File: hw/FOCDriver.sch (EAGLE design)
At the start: 113 parts, among them IC1 LM258DR2G, IC2 LM258DR2G, Q1 BC817, Q2 BC817, Q3 BC817, Q4 BC817, Q5 BC817, Q6 BC817, U1 SN74LVC2G17, U2 AO4606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

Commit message: LMV321
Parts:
- removed IC1, IC2: LM258DR2G, SparkFun-IC-Amplifiers:OPAMP-DUALU
- added C27, C28: 0.1uF, SparkFun-Capacitors:1.0UF-0805-25V-10%
- added U10, U11, U8, U9: LMV321SQ3T2G, LMV321SQ3T2G:LMV321SQ3T2G
- R23: value 1K 1% -> 5.6K
- R24: value 1K 1% -> 10K; device SparkFun-Resistors:RESISTOR0805 -> pot:TRIM_US-CT6
- R35, R36: value 10K 1% -> 1K 1%
- R46: value 5.6K -> 220
- R47: value 10K -> 10K 1%; device pot:TRIM_US-CT6 -> SparkFun-Resistors:RESISTOR0805
- R48: value 220 -> 10K 1%
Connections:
- net 5V: now also R23.2; no longer R46.2
- net AGND: now also C27.2, C28.2, R48.1, U10.GND, U11.GND, U8.GND, U9.GND; no longer IC1G3.P$V-, IC2G3.P$V-, R36.1
- net DGND: now also R24.A; no longer R47.A
- net GND: now also R29.1; no longer R27.1
- net H1O: now also R46.2; no longer R48.2
- net ICOM: now also R27.1, R30.1; no longer R23.1, R28.1
- net IU: now also R26.1; no longer R24.1
- net IV: now also R28.1; no longer R26.1
- net N$11: now also R25.2, R31.1; no longer R23.2, R29.1
- net N$12: now also R26.2, R32.1; no longer R24.2, R30.1
- net N$13: now also R31.2, U8.-IN; no longer IC2G2.-IN, R29.2
- net N$14: now also R27.2, R33.1; no longer R25.2, R31.1
- net N$15: now also R32.2, R40.1, U8.+IN; no longer IC2G2.+IN, R30.2, R41.1
- net N$16: now also U8.OUT; no longer IC2G2.OUT
- net N$17: now also R28.2, R34.1; no longer R26.2, R32.1
- net N$18: now also C27.1, R47.1, R48.2, U11.+IN; no longer C18.1, IC1G2.+IN, R35.1, R36.2
- net N$19: now also R33.2, U9.-IN; no longer IC1G1.-IN, R31.2
- net N$20: now also R34.2, R41.1, U9.+IN; no longer IC1G1.+IN, R32.2, R42.1
- net N$21: now also U9.OUT; no longer IC1G1.OUT
- net N$22: now also R29.2, R35.1; no longer R27.2, R33.1
- net N$23: now also R30.2, R36.1; no longer R28.2, R34.1
- net N$24: now also R35.2, U10.-IN; no longer IC2G1.-IN, R33.2
- net N$25: now also R36.2, R42.1, U10.+IN; no longer IC2G1.+IN, R34.2, R40.1
- net N$26: now also U10.OUT; no longer IC2G1.OUT
- net N$33: now also R46.1; no longer R48.1
- net N$4: now also R23.1, R24.E; no longer R46.1, R47.E
- net POT: now also R24.S; no longer R47.S
- net PWRDIV: now also R47.2; no longer R35.2
- net VDDA: now also C18.1, C28.1, U10.VCC, U11.VCC, U8.VCC, U9.VCC; no longer IC1G3.P$V+, IC2G3.P$V+
- net VREF: now also U11.-IN, U11.OUT; no longer IC1G2.-IN, IC1G2.OUT
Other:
- moved on the sheet: C17, C18, C19, C20, C23, C24, C26, R23, R25, R26, R27, R28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

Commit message: layout
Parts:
- removed J7: (no value), SparkFun-Connectors:CONN_06SILK_FEMALE_PTH
- added J10: (no value), SparkFun-Connectors:CONN_02
- added J11: (no value), SparkFun-Connectors:CONN_05
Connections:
- net DGND: now also J10.2, J11.5; no longer J7.6
- net IMOTORA: now also J11.3; no longer J7.3
- net IMOTORB: now also J11.1; no longer J7.1
- net IMOTORBUS: now also J11.2; no longer J7.2
- net LEDJP1: now also J10.1; no longer J7.5
- net POT: now also J11.4; no longer J7.4
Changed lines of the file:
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@@
 <clearance class="4" value="0.3048"/>
+</class>
+<class number="5" name="5V" width="0.508" drill="0.4064">
+<clearance class="5" value="0.3048"/>
 </class>
 </classes>
@@
 <part name="C7" library="SparkFun-Capacitors" deviceset="1.0UF" device="-0805-25V-10%" value="0.1uF"/>
 <part name="C4" library="SparkFun-Capacitors" deviceset="1.0UF" device="-0805-25V-10%" value="0.1uF"/>
-<part name="J7" library="SparkFun-Connectors" deviceset="CONN_06" device="SILK_FEMALE_PTH"/>
 <part name="C5" library="rcl" deviceset="CPOL-US" device="E5-10.5" value="220uF/63V"/>
 <part name="C11" library="rcl" deviceset="CPOL-US" device="E5-10.5" value="220uF/63V"/>
@@
 <part name="G10" library="SparkFun-PowerSymbols" deviceset="AGND" device=""/>
 <part name="C28" library="SparkFun-Capacitors" deviceset="1.0UF" device="-0805-25V-10%" value="0.1uF"/>
+<part name="J10" library="SparkFun-Connectors" deviceset="CONN_02" device=""/>
+<part name="GND23" library="SparkFun-PowerSymbols" deviceset="DGND" device=""/>
+<part name="J11" library="SparkFun-Connectors" deviceset="CONN_05" device=""/>
 </parts>
 <sheets>
@@
 <instance part="C7" gate="G$1" x="99.06" y="53.34"/>
 <instance part="C4" gate="G$1" x="60.96" y="53.34"/>
-<instance part="J7" gate="G$1" x="226.06" y="68.58" rot="R180"/>
 <instance part="C5" gate="G$1" x="76.2" y="157.48"/>
 <instance part="C11" gate="G$1" x="152.4" y="157.48"/>
@@
 <instance part="X2" gate="-2" x="193.04" y="48.26" rot="R180"/>
 <instance part="X2" gate="-3" x="193.04" y="53.34" rot="R180"/>
+<instance part="J10" gate="G$1" x="195.58" y="68.58" rot="R180"/>
+<instance part="GND23" gate="G$1" x="182.88" y="60.96"/>
+<instance part="J11" gate="G$1" x="228.6" y="68.58" rot="R180"/>
 </instances>
 <busses>
@@
 <segment>
 <pinref part="GND18" gate="G$1" pin="GND"/>
-<wire x1="213.36" y1="58.42" x2="213.36" y2="60.96" width="0.1524" layer="91"/>
-<pinref part="J7" gate="G$1" pin="6"/>
-<wire x1="213.36" y1="60.96" x2="220.98" y2="60.96" width="0.1524" layer="91"/>
+<wire x1="213.36" y1="58.42" x2="213.36" y2="63.5" width="0.1524" layer="91"/>
+<wire x1="213.36" y1="63.5" x2="220.98" y2="63.5" width="0.1524" layer="91"/>
+<pinref part="J11" gate="G$1" pin="5"/>
 </segment>
 <segment>
@@
 <wire x1="205.74" y1="96.52" x2="205.74" y2="99.06" width="0.1524" layer="91"/>
 <pinref part="GND17" gate="G$1" pin="GND"/>
+</segment>
+<segment>
+<pinref part="J10" gate="G$1" pin="2"/>
+<pinref part="GND23" gate="G$1" pin="GND"/>
+<wire x1="187.96" y1="66.04" x2="182.88" y2="66.04" width="0.1524" layer="91"/>
+<wire x1="182.88" y1="66.04" x2="182.88" y2="63.5" width="0.1524" layer="91"/>
 </segment>
 </net>
@@
 <label x="215.9" y="73.66" size="1.27" layer="95" rot="R180" xref="yes"/>
 <wire x1="215.9" y1="73.66" x2="220.98" y2="73.66" width="0.1524" layer="91"/>
-<pinref part="J7" gate="G$1" pin="1"/>
+<pinref part="J11" gate="G$1" pin="1"/>
 </segment>
 </net>
@@
 <label x="215.9" y="68.58" size="1.27" layer="95" rot="R180" xref="yes"/>
 <wire x1="215.9" y1="68.58" x2="220.98" y2="68.58" width="0.1524" layer="91"/>
-<pinref part="J7" gate="G$1" pin="3"/>
+<pinref part="J11" gate="G$1" pin="3"/>
 </segment>
 </net>
@@
 <label x="215.9" y="66.04" size="1.27" layer="95" rot="R180" xref="yes"/>
 <wire x1="215.9" y1="66.04" x2="220.98" y2="66.04" width="0.1524" layer="91"/>
-<pinref part="J7" gate="G$1" pin="4"/>
+<pinref part="J11" gate="G$1" pin="4"/>
 </segment>
 </net>
@@
 <wire x1="220.98" y1="71.12" x2="215.9" y2="71.12" width="0.1524" layer="91"/>
 <label x="215.9" y="71.12" size="1.27" layer="95" rot="R180" xref="yes"/>
-<pinref part="J7" gate="G$1" pin="2"/>
+<pinref part="J11" gate="G$1" pin="2"/>
 </segment>
 </net>
 <net name="LEDJP1" class="0">
 <segment>
-<label x="215.9" y="63.5" size="1.27" layer="95" rot="R180" xref="yes"/>
-<wire x1="215.9" y1="63.5" x2="220.98" y2="63.5" width="0.1524" layer="91"/>
-<pinref part="J7" gate="G$1" pin="5"/>
+<label x="182.88" y="68.58" size="1.27" layer="95" rot="R180" xref="yes"/>
+<pinref part="J10" gate="G$1" pin="1"/>
+<wire x1="182.88" y1="68.58" x2="187.96" y2="68.58" width="0.1524" layer="91"/>
 </segment>
 </net>
@@
 </segment>
 </net>
-<net name="5V" class="1">
+<net name="5V" class="5">
 <segment>
 <wire x1="86.36" y1="66.04" x2="99.06" y2="66.04" width="0.1524" layer="91"/>
@@
 </segment>
 </net>
-<net name="5V" class="1">
+<net name="5V" class="5">
 <segment>
 <pinref part="R23" gate="G$1" pin="2"/>

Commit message: layout
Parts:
- removed J11: (no value), SparkFun-Connectors:CONN_05
- added J7: (no value), SparkFun-Connectors:CONN_02
- J10: device SparkFun-Connectors:CONN_02 -> SparkFun-Connectors:CONN_04
- J9: device SparkFun-Connectors:CONN_04 -> SparkFun-Connectors:CONN_05
- R46, R49, R50, R51, R52, R53: value 220 -> 330
- renumbered LED1 to 5V
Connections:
- removed net LEDJP1: J10.1, LED2.C, LED3.C, LED4.C, LED5.C, LED6.C, LED7.C
- new net LEDON: J7.1, LED2.C, LED3.C, LED4.C, LED5.C, LED6.C, LED7.C
- net 3V3FROMMCU: now also J10.1, J10.2; no longer J9.1, J9.2
- net DGND: now also J7.2, J9.5; no longer J10.2, J11.5
- net IMOTORA: now also J9.3; no longer J11.3
- net IMOTORB: now also J9.1; no longer J11.1
- net IMOTORBUS: now also J9.2; no longer J11.2
- net POT: now also J9.4; no longer J11.4
- net PWRDIV: now also J10.3; no longer J9.3
- net VDDA: now also J10.4; no longer J9.4

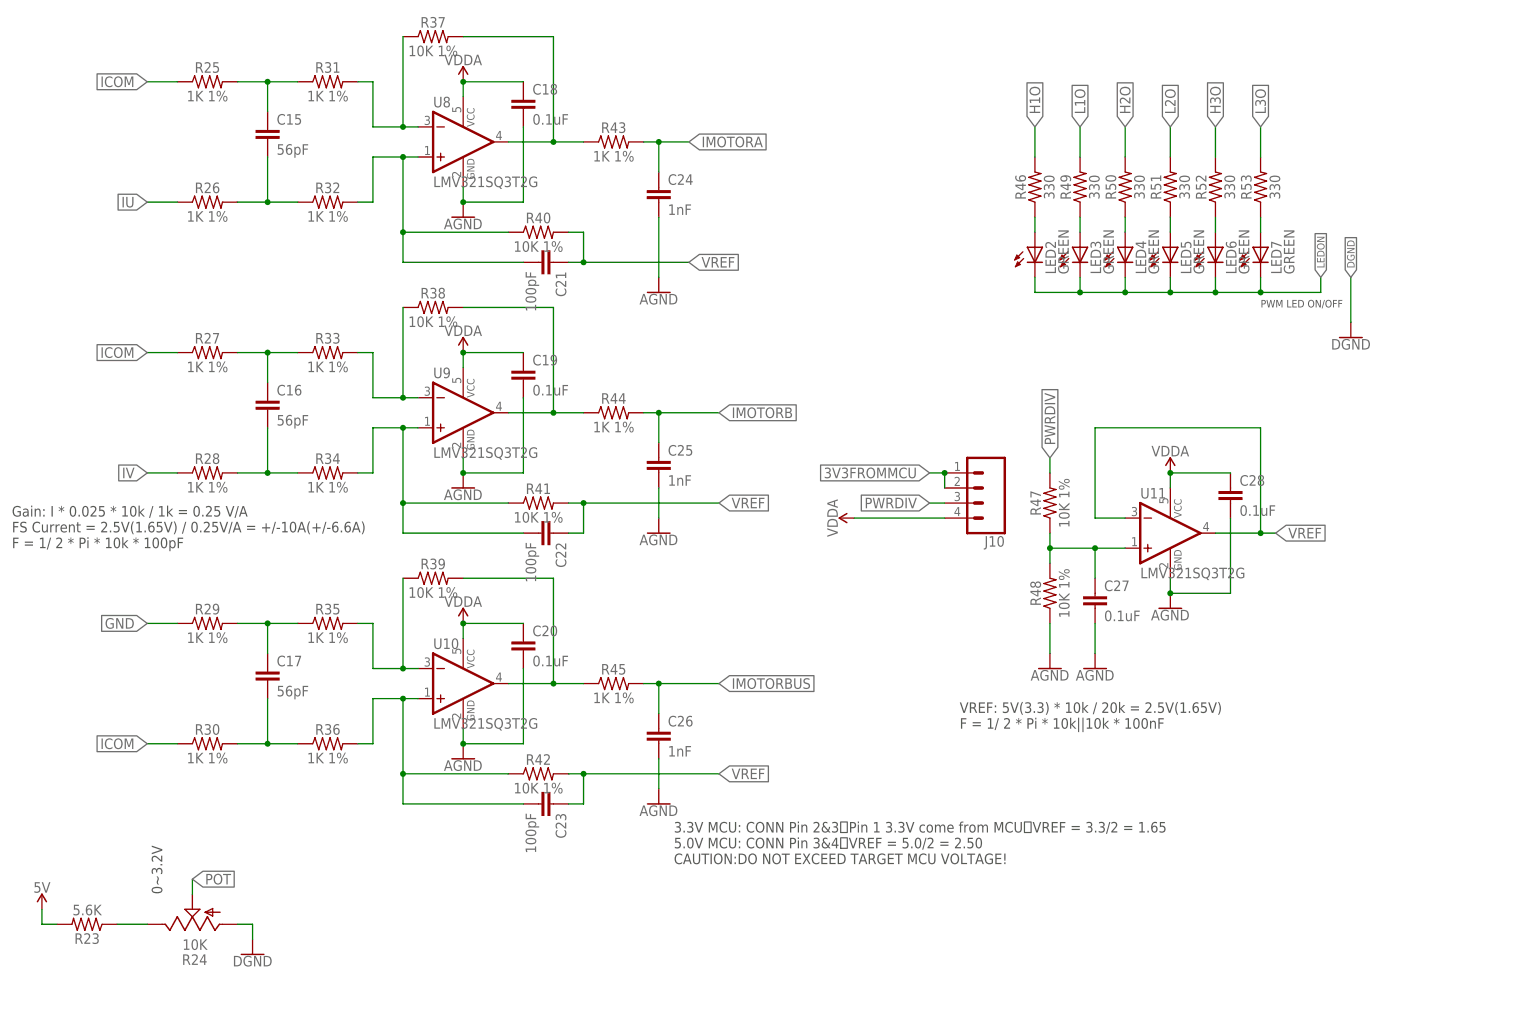
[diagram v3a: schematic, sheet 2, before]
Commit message: correct op gain
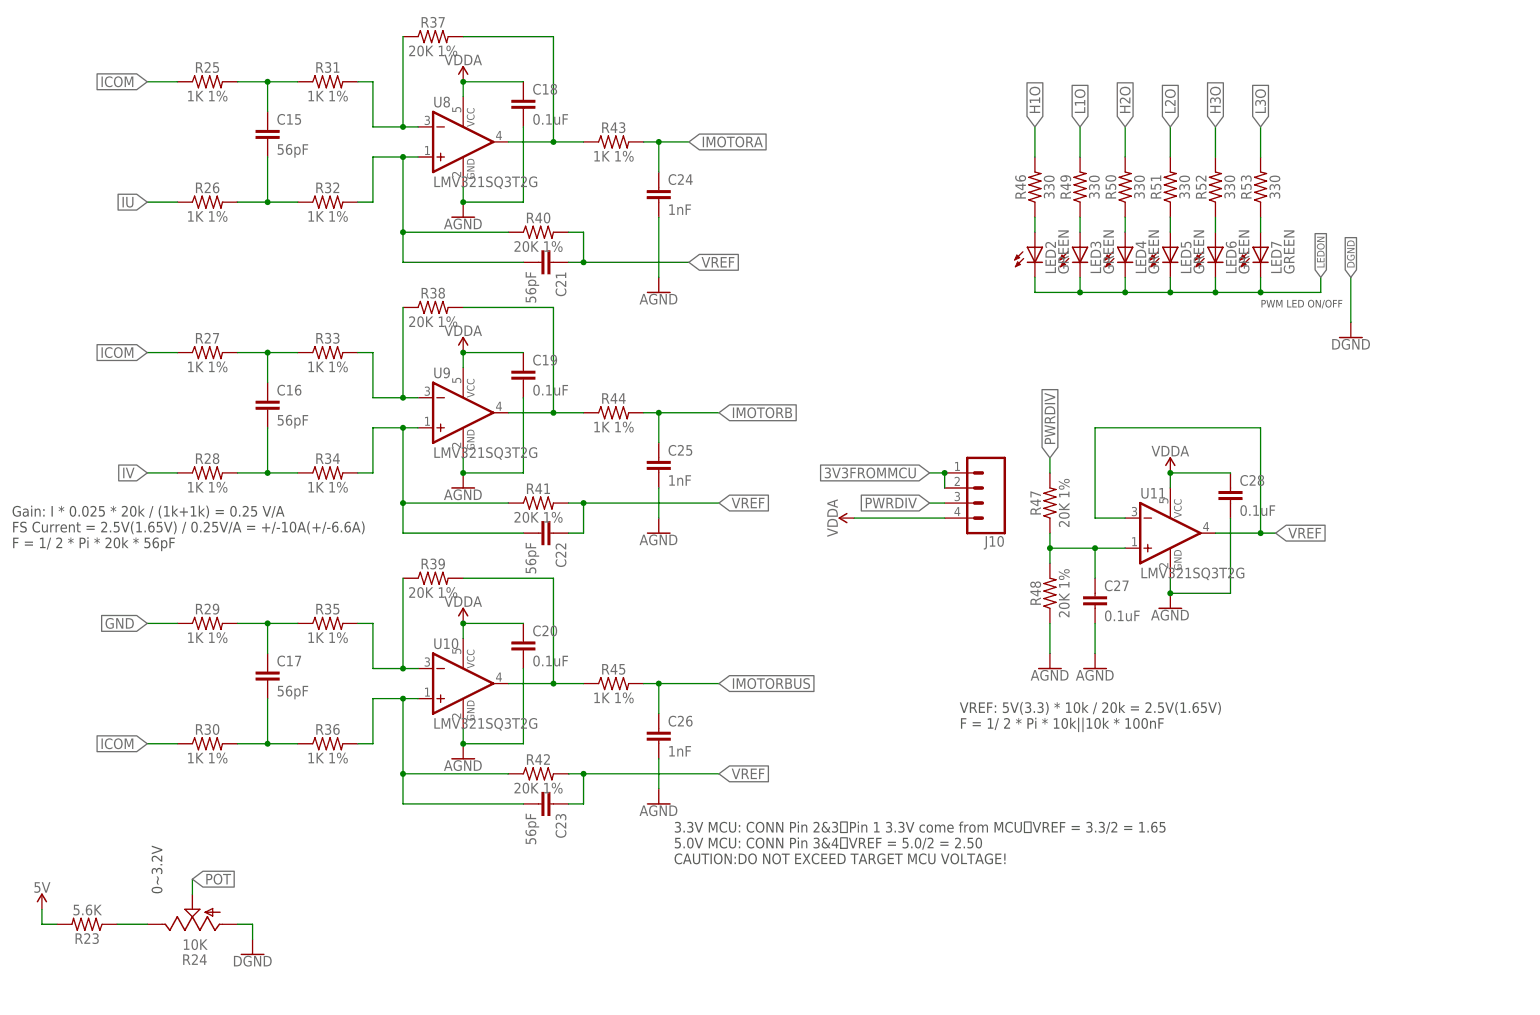
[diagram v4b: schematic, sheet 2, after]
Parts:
- C21, C22, C23: value 100pF -> 56pF
- R37, R38, R39, R40, R41, R42, R47, R48: value 10K 1% -> 20K 1%
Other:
- note added: "Gain: I * 0.025 * 20k / (1k+1k) = 0.25 V/A FS Current = 2.5V(1.65V) / 0.25V/A = +/-10A(+/-6.6A) F = 1/ 2 * Pi * 20k * 56pF"
- note removed: "Gain: I * 0.025 * 10k / 1k = 0.25 V/A FS Current = 2.5V(1.65V) / 0.25V/A = +/-10A(+/-6.6A) F = 1/ 2 * Pi * 10k * 100pF"
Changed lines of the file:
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@@
 <part name="C16" library="SparkFun-Capacitors" deviceset="1.0UF" device="-0805-25V-10%" value="56pF"/>
 <part name="C17" library="SparkFun-Capacitors" deviceset="1.0UF" device="-0805-25V-10%" value="56pF"/>
-<part name="R47" library="SparkFun-Resistors" deviceset="RESISTOR" device="0805" value="10K 1%"/>
-<part name="R48" library="SparkFun-Resistors" deviceset="RESISTOR" device="0805" value="10K 1%"/>
+<part name="R47" library="SparkFun-Resistors" deviceset="RESISTOR" device="0805" value="20K 1%"/>
+<part name="R48" library="SparkFun-Resistors" deviceset="RESISTOR" device="0805" value="20K 1%"/>
 <part name="R25" library="SparkFun-Resistors" deviceset="RESISTOR" device="0805" value="1K 1%"/>
 <part name="R26" library="SparkFun-Resistors" deviceset="RESISTOR" device="0805" value="1K 1%"/>
@@
 <part name="R35" library="SparkFun-Resistors" deviceset="RESISTOR" device="0805" value="1K 1%"/>
 <part name="R36" library="SparkFun-Resistors" deviceset="RESISTOR" device="0805" value="1K 1%"/>
-<part name="R37" library="SparkFun-Resistors" deviceset="RESISTOR" device="0805" value="10K 1%"/>
-<part name="R40" library="SparkFun-Resistors" deviceset="RESISTOR" device="0805" value="10K 1%"/>
-<part name="R38" library="SparkFun-Resistors" deviceset="RESISTOR" device="0805" value="10K 1%"/>
-<part name="R41" library="SparkFun-Resistors" deviceset="RESISTOR" device="0805" value="10K 1%"/>
-<part name="R39" library="SparkFun-Resistors" deviceset="RESISTOR" device="0805" value="10K 1%"/>
-<part name="R42" library="SparkFun-Resistors" deviceset="RESISTOR" device="0805" value="10K 1%"/>
+<part name="R37" library="SparkFun-Resistors" deviceset="RESISTOR" device="0805" value="20K 1%"/>
+<part name="R40" library="SparkFun-Resistors" deviceset="RESISTOR" device="0805" value="20K 1%"/>
+<part name="R38" library="SparkFun-Resistors" deviceset="RESISTOR" device="0805" value="20K 1%"/>
+<part name="R41" library="SparkFun-Resistors" deviceset="RESISTOR" device="0805" value="20K 1%"/>
+<part name="R39" library="SparkFun-Resistors" deviceset="RESISTOR" device="0805" value="20K 1%"/>
+<part name="R42" library="SparkFun-Resistors" deviceset="RESISTOR" device="0805" value="20K 1%"/>
 <part name="C27" library="SparkFun-Capacitors" deviceset="1.0UF" device="-0805-25V-10%" value="0.1uF"/>
-<part name="C22" library="SparkFun-Capacitors" deviceset="1.0UF" device="-0805-25V-10%" value="100pF"/>
-<part name="C23" library="SparkFun-Capacitors" deviceset="1.0UF" device="-0805-25V-10%" value="100pF"/>
-<part name="C21" library="SparkFun-Capacitors" deviceset="1.0UF" device="-0805-25V-10%" value="100pF"/>
+<part name="C22" library="SparkFun-Capacitors" deviceset="1.0UF" device="-0805-25V-10%" value="56pF"/>
+<part name="C23" library="SparkFun-Capacitors" deviceset="1.0UF" device="-0805-25V-10%" value="56pF"/>
+<part name="C21" library="SparkFun-Capacitors" deviceset="1.0UF" device="-0805-25V-10%" value="56pF"/>
 <part name="C3" library="rcl" deviceset="CPOL-US" device="E2.5-7" value="47uF/50V"/>
 <part name="X1" library="con-wago-508" deviceset="W237-02P" device=""/>
@@
 <sheet>
 <plain>
-<text x="15.24" y="81.28" size="1.778" layer="97">Gain: I * 0.025 * 10k / 1k = 0.25 V/A
+<text x="15.24" y="81.28" size="1.778" layer="97">Gain: I * 0.025 * 20k / (1k+1k) = 0.25 V/A
 FS Current = 2.5V(1.65V) / 0.25V/A = +/-10A(+/-6.6A)
-F = 1/ 2 * Pi * 10k * 100pF</text>
+F = 1/ 2 * Pi * 20k * 56pF</text>
 <text x="175.26" y="50.8" size="1.778" layer="97">VREF: 5V(3.3) * 10k / 20k = 2.5V(1.65V)
 F = 1/ 2 * Pi * 10k||10k * 100nF</text>

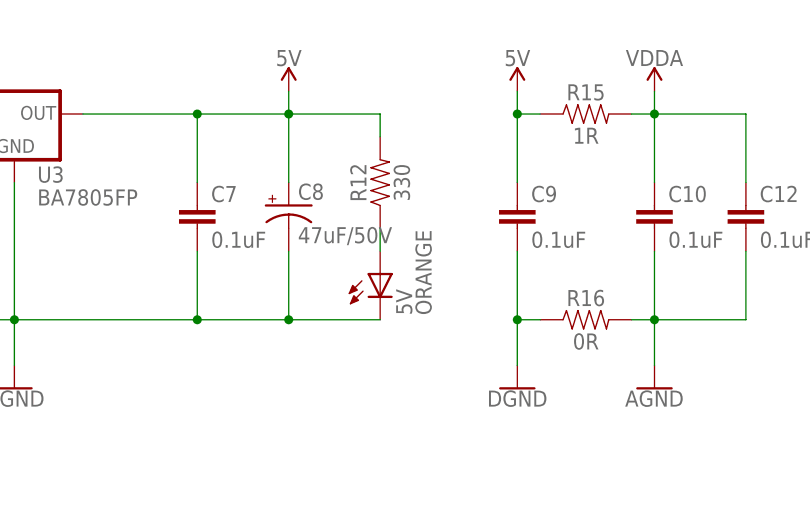
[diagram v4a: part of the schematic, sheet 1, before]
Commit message: refine top silk
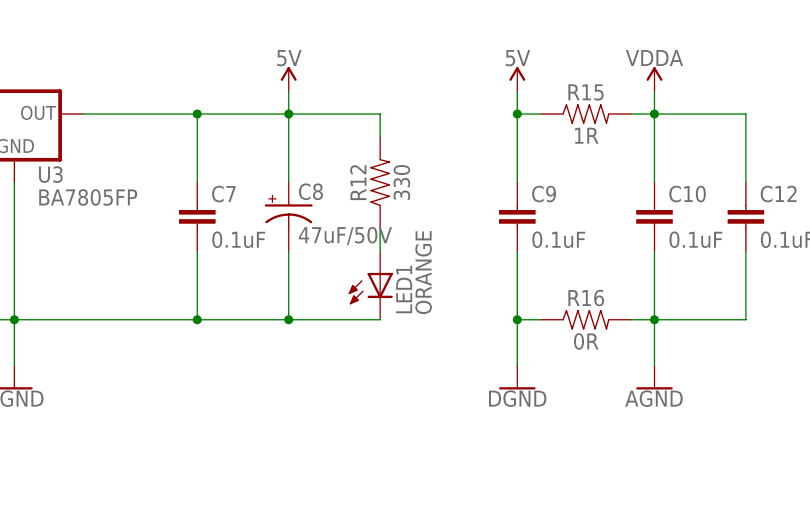
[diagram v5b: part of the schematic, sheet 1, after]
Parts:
- renumbered 5V to LED1
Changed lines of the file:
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@@
 <part name="FRAME1" library="frames" deviceset="A4L-LOC" device=""/>
 <part name="FRAME2" library="frames" deviceset="A4L-LOC" device=""/>
-<part name="5V" library="led" deviceset="LED" device="SML0805" value="ORANGE"/>
+<part name="LED1" library="led" deviceset="LED" device="SML0805" value="ORANGE"/>
 <part name="R1" library="SparkFun-Resistors" deviceset="RESISTOR" device="0805" value="1K"/>
 <part name="R3" library="SparkFun-Resistors" deviceset="RESISTOR" device="0805" value="1K"/>
@@
 <instance part="U3" gate="G$1" x="78.74" y="66.04"/>
 <instance part="F1" gate="G$1" x="30.48" y="66.04"/>
-<instance part="5V" gate="G$1" x="119.38" y="48.26"/>
+<instance part="LED1" gate="G$1" x="119.38" y="48.26"/>
 <instance part="R12" gate="G$1" x="119.38" y="58.42" rot="R90"/>
 <instance part="R15" gate="G$1" x="142.24" y="66.04"/>
@@
 </segment>
 <segment>
-<pinref part="5V" gate="G$1" pin="C"/>
+<pinref part="LED1" gate="G$1" pin="C"/>
 <pinref part="C8" gate="G$1" pin="-"/>
 <wire x1="78.74" y1="43.18" x2="78.74" y2="58.42" width="0.1524" layer="91"/>
@@
 <net name="N$31" class="0">
 <segment>
-<pinref part="5V" gate="G$1" pin="A"/>
+<pinref part="LED1" gate="G$1" pin="A"/>
 <wire x1="119.38" y1="50.8" x2="119.38" y2="53.34" width="0.1524" layer="91"/>
 <pinref part="R12" gate="G$1" pin="1"/>
